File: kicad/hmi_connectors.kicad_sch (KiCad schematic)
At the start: 6 parts, among them J21 Arduino UNO Q Shield Header

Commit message: fix: Resolve 5 ERC warnings — footprints, grid alignment, net conflict
1. Inductor footprint: L_4.0x4.0mm_H2.0mm → L_Taiyo-Yuden_NR-40xx
   (power_management.kicad_sch)

2. Relay footprint (×2): Relay_SPST_HF46F → Relay_SPDT_Omron_G5V-1
   (actuator_drivers.kicad_sch — K1, K2)

3. Off-grid coordinates: TPS3823 symbol and WDT_RESET label moved
   from 300.48/310.64 to 300.99/311.15 (1.27mm grid aligned)
   PWR_FLAG reference position 28.575 → 27.94
   (power_management.kicad_sch)

4. HUM_ADC/I2C_SDA overlap: Both hierarchical labels were at same
   coordinates (55.88, 107.95). Shifted I2C_SDA and downstream
   labels down by 2.54mm each to eliminate net conflict.
   (hmi_connectors.kicad_sch)

Co-Authored-By: Devin AI <158243242+devin-ai-integration[bot]@users.noreply.github.com>
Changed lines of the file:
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@@
   (hierarchical_label "TEMP_ADC"    (shape input) (at 55.88 105.41 180) (effects (font (size 1.27 1.27))))
   (hierarchical_label "HUM_ADC"     (shape input) (at 55.88 107.95 180) (effects (font (size 1.27 1.27))))
-  (hierarchical_label "I2C_SDA"     (shape bidirectional) (at 55.88 107.95 180) (effects (font (size 1.27 1.27))))
-  (hierarchical_label "I2C_SCL"     (shape bidirectional) (at 55.88 110.49 180) (effects (font (size 1.27 1.27))))
+  (hierarchical_label "I2C_SDA"     (shape bidirectional) (at 55.88 110.49 180) (effects (font (size 1.27 1.27))))
+  (hierarchical_label "I2C_SCL"     (shape bidirectional) (at 55.88 113.03 180) (effects (font (size 1.27 1.27))))
   (hierarchical_label "HX711_DOUT"  (shape input) (at 121.92 138.43 0)  (effects (font (size 1.27 1.27))))
   (hierarchical_label "HX711_SCK"   (shape output)(at 121.92 135.89 0)  (effects (font (size 1.27 1.27))))
@@
   (hierarchical_label "HMI_RX"      (shape input) (at 121.92 146.05 0)  (effects (font (size 1.27 1.27))))
   (hierarchical_label "MCU_WDI"     (shape output)(at 121.92 148.59 0)  (effects (font (size 1.27 1.27))))
-  (hierarchical_label "MCU_NRST"    (shape input) (at 55.88 112.39 180) (effects (font (size 1.27 1.27))))
-  (hierarchical_label "5V_RAIL"     (shape bidirectional)(at 55.88 117.48 180) (effects (font (size 1.27 1.27))))
-  (hierarchical_label "3V3_RAIL"    (shape bidirectional)(at 55.88 115.57 180) (effects (font (size 1.27 1.27))))
+  (hierarchical_label "MCU_NRST"    (shape input) (at 55.88 115.57 180) (effects (font (size 1.27 1.27))))
+  (hierarchical_label "5V_RAIL"     (shape bidirectional)(at 55.88 120.65 180) (effects (font (size 1.27 1.27))))
+  (hierarchical_label "3V3_RAIL"    (shape bidirectional)(at 55.88 118.11 180) (effects (font (size 1.27 1.27))))
   (hierarchical_label "12V_RAIL"    (shape input)  (at 10.16 25.4 0)    (effects (font (size 1.27 1.27))))
-  (hierarchical_label "GND"         (shape bidirectional)(at 55.88 119.38 180) (effects (font (size 1.27 1.27))))
+  (hierarchical_label "GND"         (shape bidirectional)(at 55.88 123.19 180) (effects (font (size 1.27 1.27))))
 )

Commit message: fix: Embed lib_symbols, fix invalid lib_ids, bump to KiCad 9 format
- Embed complete (lib_symbols) definitions in all 5 sub-sheets so symbols
  render as real parts instead of '??' placeholders (files now self-contained)
- Substitute invalid lib_ids with valid library symbols:
  Device:CP -> Device:C_Polarized, Diode:PESD3V3S2USF -> Diode:PESD3V3S1UL,
  Diode:PESD5V0S1BSF -> Diode:PESD5V0S1UL, Isolator:PC817X2 -> Isolator:PC817
- Bump file format version 20231120 -> 20250114 (removes 'older version' warning)
- Left-justify header text blocks so long lines stay within the A3 frame

Validated: kicad-cli SVG render (all real symbols, within frame), clean-room
eeschema GUI render with broken library table (no '??'), and kicad-cli ERC
runs without crashing (425 violations are expected unconnected-pin/dangling-
label items, resolved during per-sheet wiring).

Co-Authored-By: Devin AI <158243242+devin-ai-integration[bot]@users.noreply.github.com>
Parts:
- D_HMI: symbol Diode:PESD3V3S2USF -> Diode:PESD3V3S1UL
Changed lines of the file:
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@@
 (kicad_sch
-  (version 20231120)
+  (version 20250114)
   (generator "devin")
   (generator_version "1.0")
@@
   (text "HMI & CONNECTORS\nHMI via UART (D0/D1) — Nextion/Stone compatible\nShield header J21 connects to Arduino UNO Q\nDC input J17 on power_management sheet"
     (at 25.4 15.24 0)
-    (effects (font (size 2.54 2.54)))
+    (effects (font (size 2.54 2.54)) (justify left))
   )
   (text "HMI DISPLAY — UART Interface\nJST-XH 4-pin: 5V / MCU_TX(D1) / MCU_RX(D0) / GND\nCompatible: Nextion, Stone, DWIN HMI panels\nProtection: TVS ESD on TX/RX lines"
@@
   )
   (symbol
-    (lib_id "Diode:PESD3V3S2USF")
+    (lib_id "Diode:PESD3V3S1UL")
     (at 86.36 50.8 0) (unit 1)
     (exclude_from_sim no) (in_bom yes) (on_board yes)

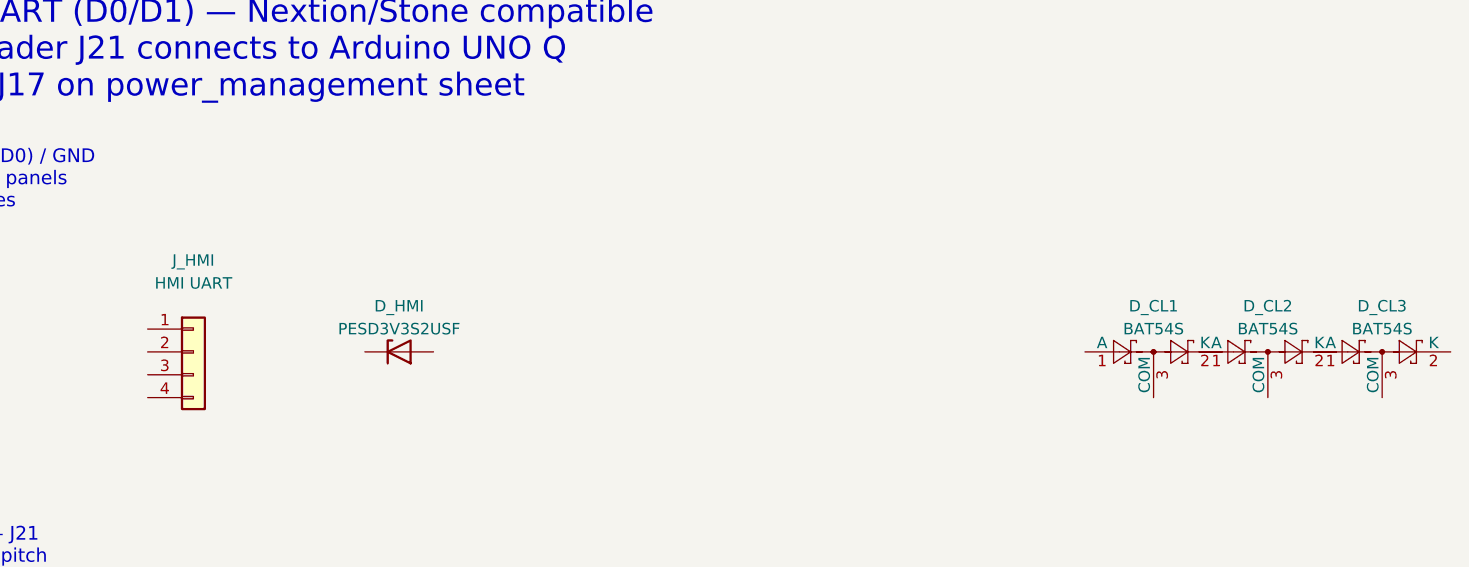
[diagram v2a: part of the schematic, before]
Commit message: fix: Re-annotate components with unique global references + add instances blocks
Root cause: symbol instances lacked (instances ...) blocks, so KiCad treated
all references as unannotated/duplicated (108 duplicate_reference ERC errors)
and produced auto-renamed names (C_DO2, U3_2A, ...) on annotation.

Fix: assign globally-unique sequential standard references (R1..R28, C1..C27,
U1..U20, D1..D18, J1..J21, etc.) and embed a proper (instances) block per
symbol with the correct hierarchical path. Each MCP6002 kept as its own IC
(unit A) to preserve per-channel galvanic isolation (pH/ORP/DO).

ERC: duplicate_reference 108 -> 0, unannotated 1 -> 0.
Co-Authored-By: Devin AI <158243242+devin-ai-integration[bot]@users.noreply.github.com>
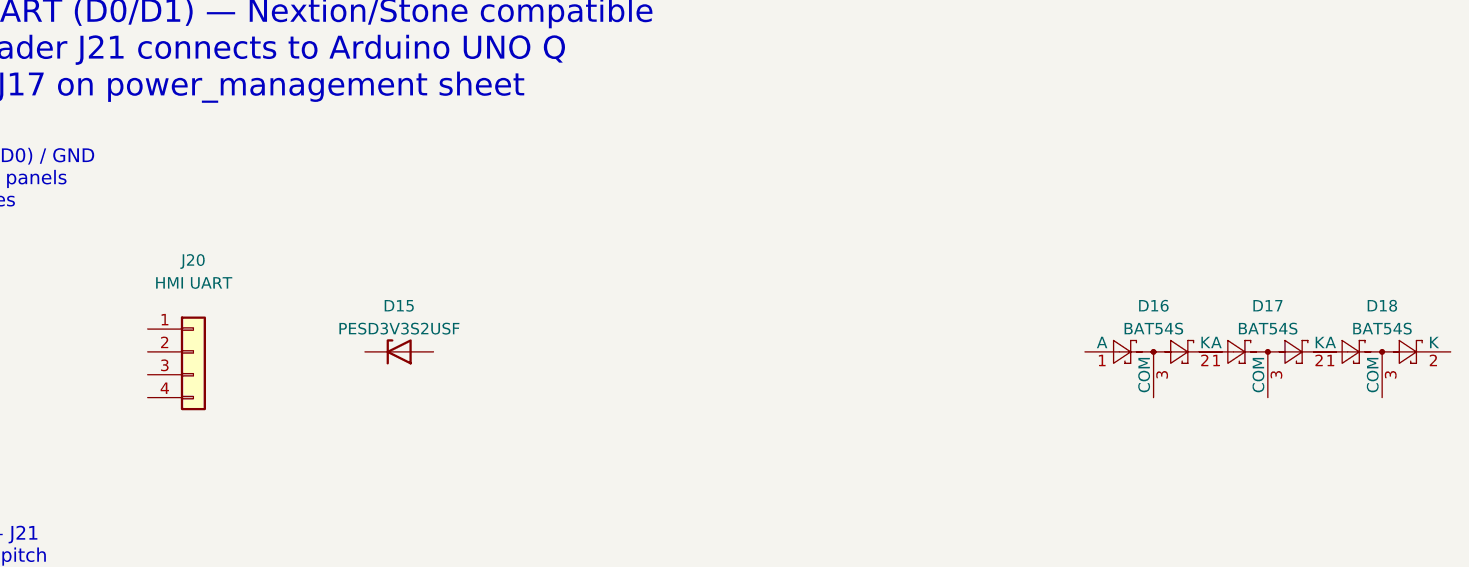
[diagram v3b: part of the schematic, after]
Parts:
- renumbered D_HMI to D15, D_CL1 to D16, D_CL2 to D17, D_CL3 to D18, J_HMI to J20
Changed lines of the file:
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@@
     (at 63.5 50.8 0) (unit 1)
     (exclude_from_sim no) (in_bom yes) (on_board yes)
-    (property "Reference" "J_HMI" (at 63.5 40.64 0) (effects (font (size 1.27 1.27))))
+    (property "Reference" "J20" (at 63.5 40.64 0) (effects (font (size 1.27 1.27))))
     (property "Value" "HMI UART" (at 63.5 43.18 0) (effects (font (size 1.27 1.27))))
     (property "Footprint" "Connector_JST:JST_XH_B4B-XH-A_1x04_P2.50mm_Vertical"
@@
     (pin "3")
     (pin "4")
+    (instances
+      (project "nebula_qshield"
+        (path "/c6da75fc-541f-4933-b134-f5eb8982a11b/f787f9da-3fea-4da5-bd0c-c3201676b3de"
+          (reference "J20") (unit 1)
+        )
+      )
+    )
   )
   (symbol
@@
     (at 86.36 50.8 0) (unit 1)
     (exclude_from_sim no) (in_bom yes) (on_board yes)
-    (property "Reference" "D_HMI" (at 86.36 45.72 0) (effects (font (size 1.27 1.27))))
+    (property "Reference" "D15" (at 86.36 45.72 0) (effects (font (size 1.27 1.27))))
     (property "Value" "PESD3V3S2USF" (at 86.36 48.26 0) (effects (font (size 1.27 1.27))))
     (property "Footprint" "Package_TO_SOT_SMD:SOT-23-3" (at 86.36 50.8 0) (effects (font (size 1.27 1.27)) hide))
     (property "MPN" "PESD3V3S2USF" (at 86.36 50.8 0) (effects (font (size 1.27 1.27)) hide))
     (pin "1") (pin "2") (pin "3")
+    (instances
+      (project "nebula_qshield"
+        (path "/c6da75fc-541f-4933-b134-f5eb8982a11b/f787f9da-3fea-4da5-bd0c-c3201676b3de"
+          (reference "D15") (unit 1)
+        )
+      )
+    )
   )
   (text "ARDUINO UNO Q SHIELD HEADER — J21\n2x20 stackable pin header, 2.54mm pitch\nAll signals routed through this connector"
@@
     (pin "37") (pin "38") (pin "39")
     (pin "40")
+    (instances
+      (project "nebula_qshield"
+        (path "/c6da75fc-541f-4933-b134-f5eb8982a11b/f787f9da-3fea-4da5-bd0c-c3201676b3de"
+          (reference "J21") (unit 1)
+        )
+      )
+    )
   )
   (symbol (lib_id "Diode:BAT54S") (at 170.18 50.8 0) (unit 1) (exclude_from_sim no) (in_bom yes) (on_board yes)
-    (property "Reference" "D_CL1" (at 170.18 45.72 0) (effects (font (size 1.27 1.27))))
+    (property "Reference" "D16" (at 170.18 45.72 0) (effects (font (size 1.27 1.27))))
     (property "Value" "BAT54S" (at 170.18 48.26 0) (effects (font (size 1.27 1.27))))
     (property "Footprint" "Package_TO_SOT_SMD:SOT-23-3" (at 170.18 50.8 0) (effects (font (size 1.27 1.27)) hide))
     (pin "1") (pin "2") (pin "3")
+    (instances
+      (project "nebula_qshield"
+        (path "/c6da75fc-541f-4933-b134-f5eb8982a11b/f787f9da-3fea-4da5-bd0c-c3201676b3de"
+          (reference "D16") (unit 1)
+        )
+      )
+    )
   )
   (symbol (lib_id "Diode:BAT54S") (at 182.88 50.8 0) (unit 1) (exclude_from_sim no) (in_bom yes) (on_board yes)
-    (property "Reference" "D_CL2" (at 182.88 45.72 0) (effects (font (size 1.27 1.27))))
+    (property "Reference" "D17" (at 182.88 45.72 0) (effects (font (size 1.27 1.27))))
     (property "Value" "BAT54S" (at 182.88 48.26 0) (effects (font (size 1.27 1.27))))
     (property "Footprint" "Package_TO_SOT_SMD:SOT-23-3" (at 182.88 50.8 0) (effects (font (size 1.27 1.27)) hide))
     (pin "1") (pin "2") (pin "3")
+    (instances
+      (project "nebula_qshield"
+        (path "/c6da75fc-541f-4933-b134-f5eb8982a11b/f787f9da-3fea-4da5-bd0c-c3201676b3de"
+          (reference "D17") (unit 1)
+        )
+      )
+    )
   )
   (symbol (lib_id "Diode:BAT54S") (at 195.58 50.8 0) (unit 1) (exclude_from_sim no) (in_bom yes) (on_board yes)
-    (property "Reference" "D_CL3" (at 195.58 45.72 0) (effects (font (size 1.27 1.27))))
+    (property "Reference" "D18" (at 195.58 45.72 0) (effects (font (size 1.27 1.27))))
     (property "Value" "BAT54S" (at 195.58 48.26 0) (effects (font (size 1.27 1.27))))
     (property "Footprint" "Package_TO_SOT_SMD:SOT-23-3" (at 195.58 50.8 0) (effects (font (size 1.27 1.27)) hide))
     (pin "1") (pin "2") (pin "3")
+    (instances
+      (project "nebula_qshield"
+        (path "/c6da75fc-541f-4933-b134-f5eb8982a11b/f787f9da-3fea-4da5-bd0c-c3201676b3de"
+          (reference "D18") (unit 1)
+        )
+      )
+    )
   )
   (hierarchical_label "PH_ADC"      (shape input) (at 55.88 95.25 180)  (effects (font (size 1.27 1.27))))

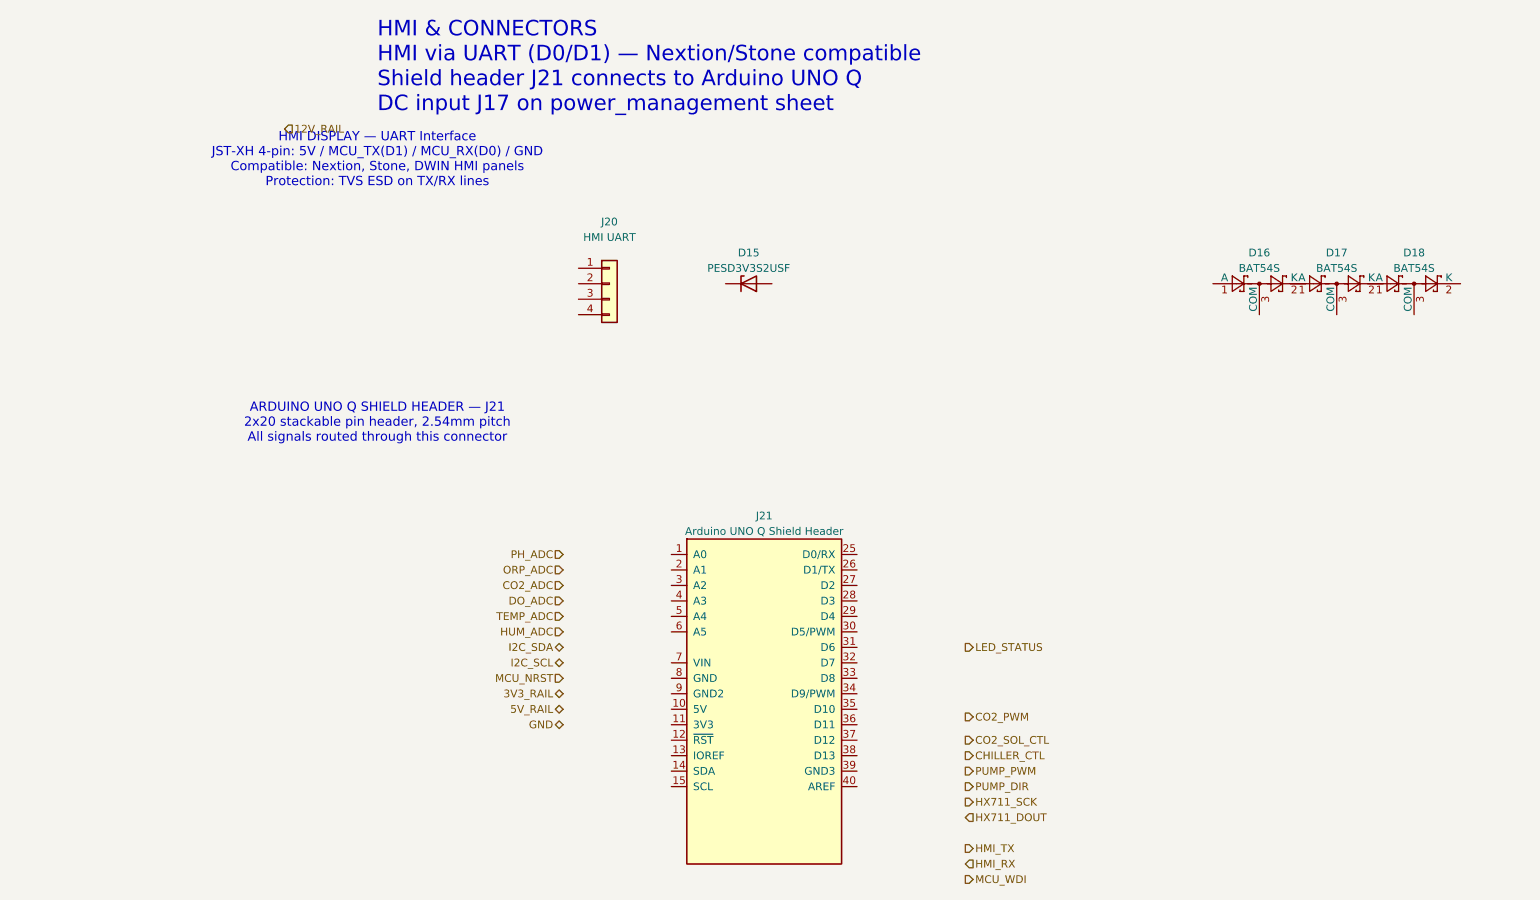
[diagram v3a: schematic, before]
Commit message: feat: Wire digital_i2c, actuator_drivers, hmi_connectors + root schematic — ERC violations 322→24 (acceptable)
Co-Authored-By: Devin AI <158243242+devin-ai-integration[bot]@users.noreply.github.com>
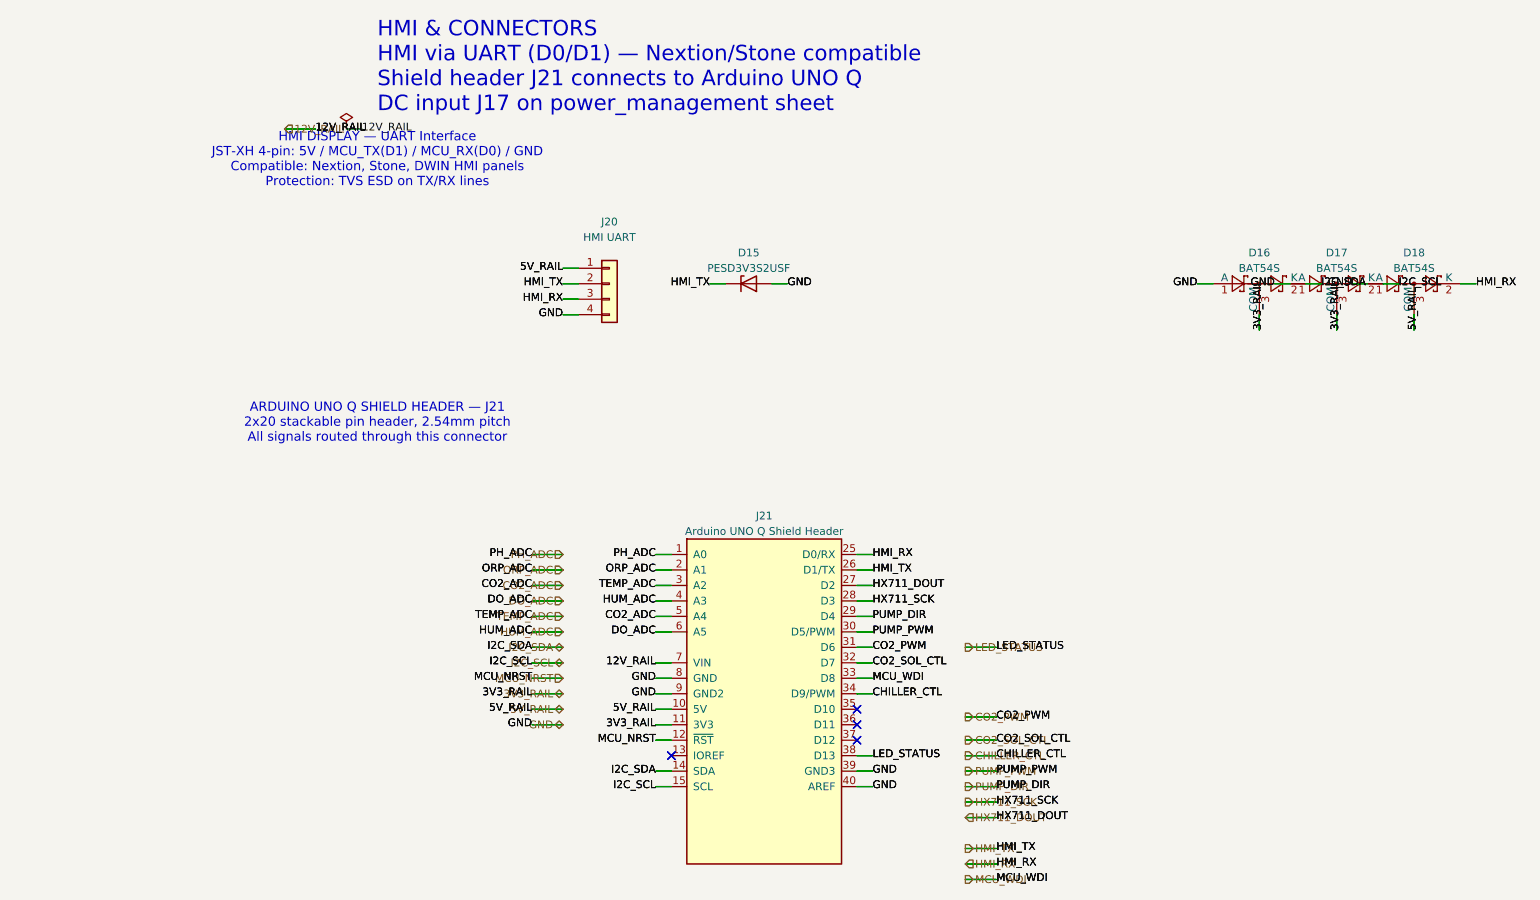
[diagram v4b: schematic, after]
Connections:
- net 12V_RAIL: now also J21.7 (VIN)
- net 3V3_RAIL: now also D16.3 (COM), D17.3 (COM), J21.11 (3V3)
- net 5V_RAIL: now also D18.3 (COM), J20.1 (Pin_1), J21.10 (5V)
- net CHILLER_CTL: now also J21.34 (D9/PWM)
- net CO2_ADC: now also J21.5 (A4)
- net CO2_PWM: now also J21.31 (D6)
- net CO2_SOL_CTL: now also J21.32 (D7)
- net DO_ADC: now also J21.6 (A5)
- net GND: now also D15.2 (A), D16.1 (A), D17.1 (A), D18.1 (A), J20.4 (Pin_4), J21.39 (GND3), J21.40 (AREF), J21.8 (GND), J21.9 (GND2)
- net HMI_RX: now also D18.2 (K), J20.3 (Pin_3), J21.25 (D0/RX)
- net HMI_TX: now also D15.1 (K), J20.2 (Pin_2), J21.26 (D1/TX)
- net HUM_ADC: now also J21.4 (A3)
- net HX711_DOUT: now also J21.27 (D2)
- net HX711_SCK: now also J21.28 (D3)
- net I2C_SCL: now also D17.2 (K), J21.15 (SCL)
- net I2C_SDA: now also D16.2 (K), J21.14 (SDA)
- net LED_STATUS: now also J21.38 (D13)
- net MCU_NRST: now also J21.12 (~{RST})
- net MCU_WDI: now also J21.33 (D8)
- net ORP_ADC: now also J21.2 (A1)
- net PH_ADC: now also J21.1 (A0)
- net PUMP_DIR: now also J21.29 (D4)
- net PUMP_PWM: now also J21.30 (D5/PWM)
- net TEMP_ADC: now also J21.3 (A2)
- no-connect marks 0 -> 8
